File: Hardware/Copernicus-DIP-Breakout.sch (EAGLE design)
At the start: 12 parts, among them U1 COPERNICUS

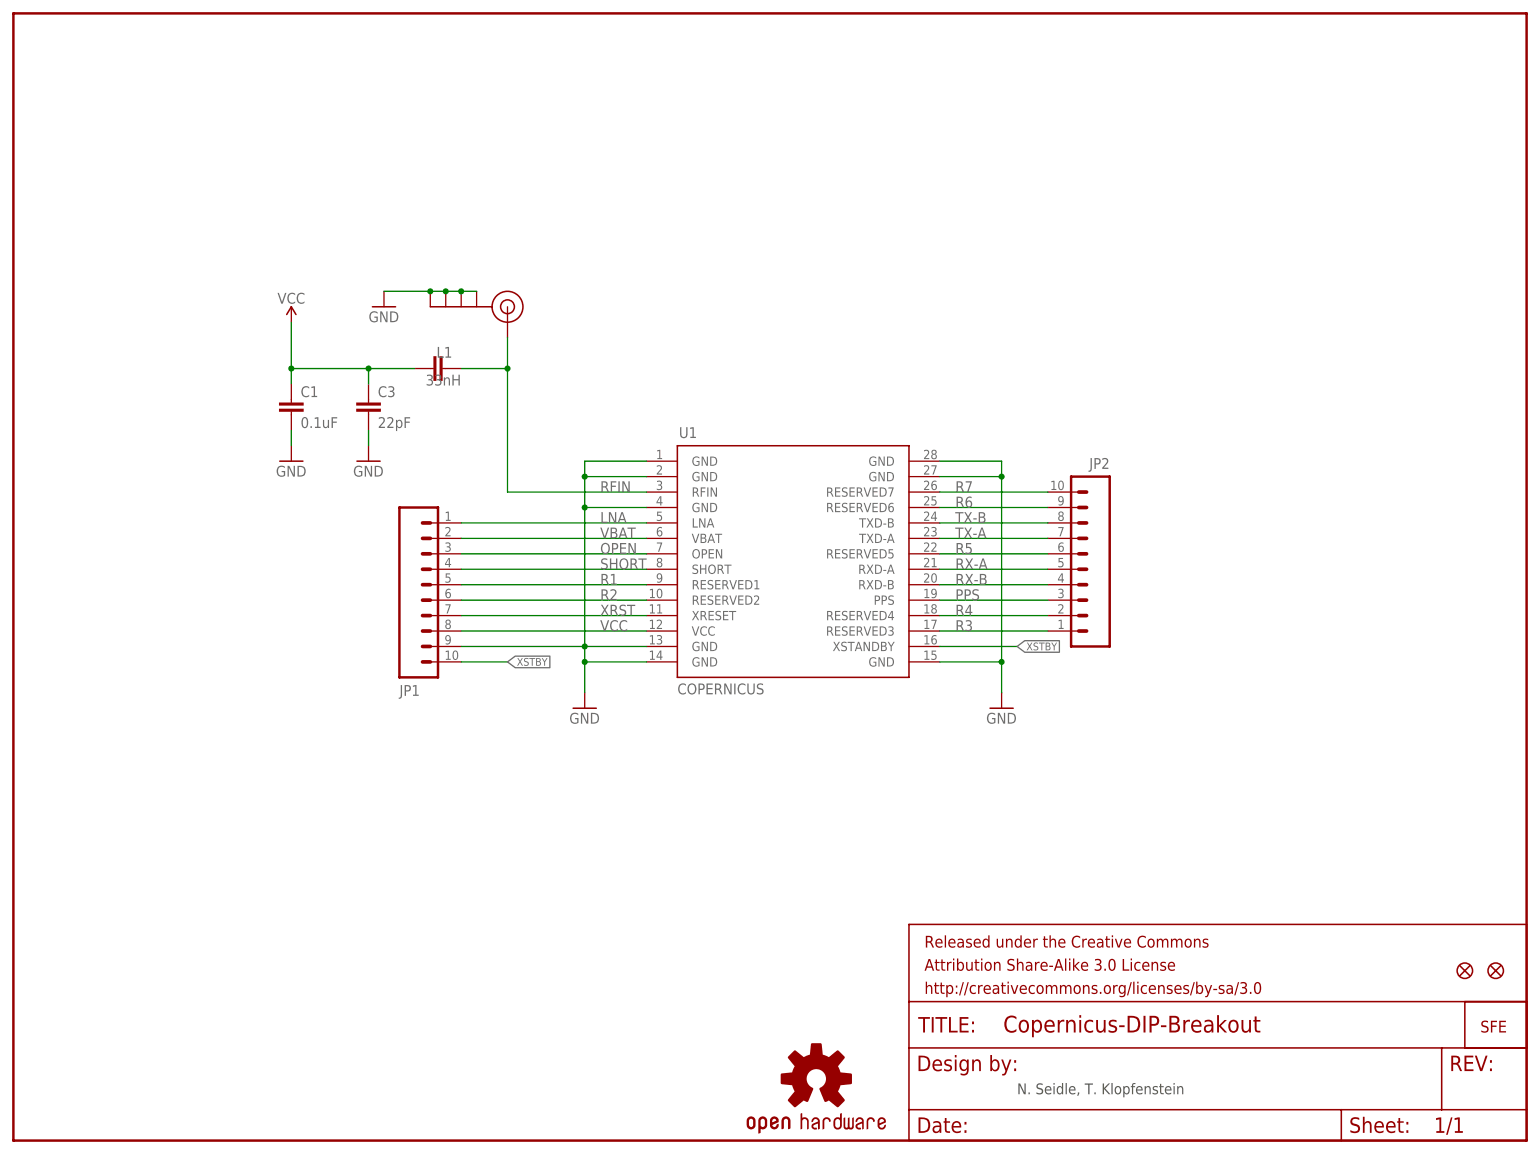
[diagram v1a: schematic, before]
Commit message: Updated board to proper pin names, added in connection between XSTBY and Vcc, changed caps and inductor to 0603 package, and decreased PCB size.
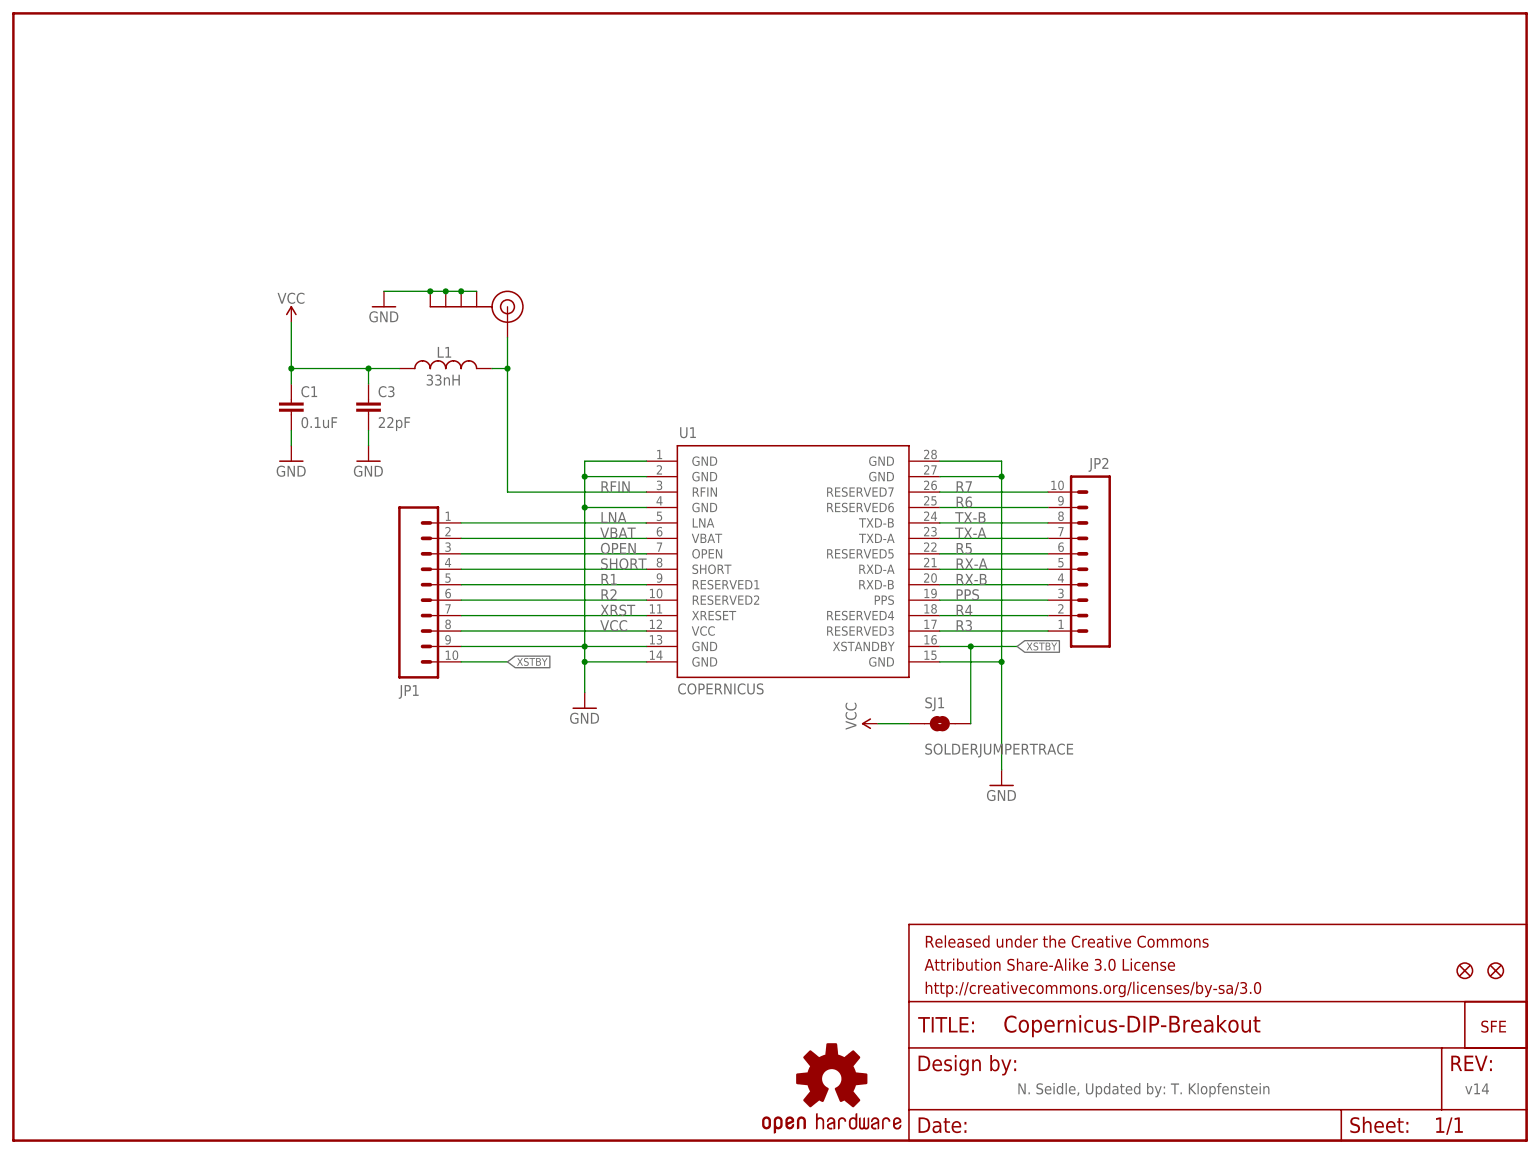
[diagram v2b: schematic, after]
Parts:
- removed LOGO1: OSHW-LOGOS, SparkFun-Aesthetics:OSHW-LOGOS
- added JP4: LOGO-SFESK, SparkFun-Aesthetics:LOGO-SFESK
- added SJ1: SOLDERJUMPERTRACE, SparkFun-Passives:SOLDERJUMPERTRACE
- C1, C3: device SparkFun:CAP0402-CAP -> SparkFun-Passives:CAP0603-CAP
- L1: device SparkFun:CAP0402-CAP -> SparkFun-Passives:INDUCTOR0603
- U$1: value LOGO-SFENEW -> OSHW-LOGOS; device SparkFun:LOGO-SFENEW -> SparkFun-Aesthetics:OSHW-LOGOS
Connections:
- net VCC: now also SJ1.1
- net XSTBY: now also SJ1.2
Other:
- note added: "N. Seidle, Updated by: T. Klopfenstein"
- note added: "v14"
- note removed: "N. Seidle, T. Klopfenstein"
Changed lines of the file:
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@@
 <parts>
 <part name="JP3" library="SparkFun-Nate" deviceset="SMA_EDGE" device=""/>
-<part name="C3" library="SparkFun" deviceset="CAP" device="0402-CAP" value="22pF"/>
-<part name="C1" library="SparkFun" deviceset="CAP" device="0402-CAP" value="0.1uF"/>
+<part name="C3" library="SparkFun-Passives" deviceset="CAP" device="0603-CAP" value="22pF"/>
+<part name="C1" library="SparkFun-Passives" deviceset="CAP" device="0603-CAP" value="0.1uF"/>
 <part name="3.3V1" library="SparkFun" deviceset="VCC" device=""/>
 <part name="GND9" library="SparkFun" deviceset="GND" device=""/>
@@
 <part name="JP2" library="SparkFun" deviceset="M10" device="&quot;" value=""/>
 <part name="U1" library="SparkFun-RF" deviceset="COPERNICUS" device="SMD" value="COPERNICUS"/>
-<part name="U$1" library="SparkFun" deviceset="LOGO-SFE" device="NEW"/>
 <part name="GND2" library="SparkFun" deviceset="GND" device=""/>
-<part name="L1" library="SparkFun" deviceset="CAP" device="0402-CAP" value="33nH"/>
+<part name="L1" library="SparkFun-Passives" deviceset="INDUCTOR" device="0603" value="33nH"/>
 <part name="U$2" library="SparkFun" deviceset="FIDUCIAL" device="1X2"/>
 <part name="U$3" library="SparkFun" deviceset="FIDUCIAL" device="1X2"/>
 <part name="GND1" library="SparkFun" deviceset="GND" device=""/>
 <part name="FRAME1" library="SparkFun-Aesthetics" deviceset="FRAME-LETTER" device=""/>
-<part name="LOGO1" library="SparkFun-Aesthetics" deviceset="OSHW-LOGO" device="S"/>
+<part name="SJ1" library="SparkFun-Passives" deviceset="SOLDERJUMPER" device="TRACE"/>
+<part name="P+1" library="SparkFun-Aesthetics" deviceset="VCC" device=""/>
+<part name="U$1" library="SparkFun-Aesthetics" deviceset="OSHW-LOGO" device="S"/>
+<part name="JP4" library="SparkFun-Aesthetics" deviceset="LOGO-SFE" device="SK"/>
 </parts>
 <sheets>
 <sheet>
 <plain>
-<text x="165.1" y="7.62" size="1.778" layer="97">N. Seidle, T. Klopfenstein</text>
+<text x="165.1" y="7.62" size="1.778" layer="96">N. Seidle, Updated by: T. Klopfenstein</text>
+<text x="238.76" y="7.62" size="1.778" layer="96">v14</text>
 </plain>
 <instances>
@@
 <attribute name="VALUE" x="109.22" y="73.406" size="1.778" layer="96"/>
 </instance>
-<instance part="U$1" gate="G$1" x="241.3" y="17.78"/>
 <instance part="GND2" gate="1" x="93.98" y="71.12"/>
 <instance part="L1" gate="G$1" x="71.12" y="127" smashed="yes" rot="R90">
@@
 <instance part="U$2" gate="G$1" x="243.84" y="27.94"/>
 <instance part="U$3" gate="G$1" x="238.76" y="27.94"/>
-<instance part="GND1" gate="1" x="162.56" y="71.12"/>
+<instance part="GND1" gate="1" x="162.56" y="58.42"/>
 <instance part="FRAME1" gate="G$1" x="0" y="0"/>
 <instance part="FRAME1" gate="G$2" x="147.32" y="0"/>
-<instance part="LOGO1" gate="G$1" x="132.08" y="10.16"/>
+<instance part="SJ1" gate="1" x="152.4" y="68.58"/>
+<instance part="P+1" gate="1" x="142.24" y="68.58" rot="R90"/>
+<instance part="U$1" gate="G$1" x="134.62" y="10.16"/>
+<instance part="JP4" gate="G$1" x="241.3" y="17.78"/>
 </instances>
 <busses>
@@
 <segment>
 <pinref part="GND1" gate="1" pin="GND"/>
-<wire x1="162.56" y1="78.74" x2="162.56" y2="73.66" width="0.1524" layer="91"/>
+<wire x1="162.56" y1="78.74" x2="162.56" y2="60.96" width="0.1524" layer="91"/>
 <wire x1="162.56" y1="78.74" x2="152.4" y2="78.74" width="0.1524" layer="91"/>
 <pinref part="U1" gate="G$2" pin="GND@6"/>
@@
 </segment>
 <segment>
-<wire x1="66.04" y1="127" x2="58.42" y2="127" width="0.1524" layer="91"/>
+<wire x1="63.5" y1="127" x2="58.42" y2="127" width="0.1524" layer="91"/>
 <wire x1="58.42" y1="127" x2="45.72" y2="127" width="0.1524" layer="91"/>
 <wire x1="45.72" y1="127" x2="45.72" y2="134.62" width="0.1524" layer="91"/>
@@
 <pinref part="L1" gate="G$1" pin="1"/>
 </segment>
+<segment>
+<pinref part="SJ1" gate="1" pin="1"/>
+<pinref part="P+1" gate="1" pin="VCC"/>
+<wire x1="142.24" y1="68.58" x2="147.32" y2="68.58" width="0.1524" layer="91"/>
+</segment>
 </net>
 <net name="RFIN" class="0">
 <segment>
 <wire x1="81.28" y1="127" x2="81.28" y2="132.08" width="0.1524" layer="91"/>
-<wire x1="73.66" y1="127" x2="81.28" y2="127" width="0.1524" layer="91"/>
+<wire x1="78.74" y1="127" x2="81.28" y2="127" width="0.1524" layer="91"/>
 <wire x1="104.14" y1="106.68" x2="81.28" y2="106.68" width="0.1524" layer="91"/>
 <wire x1="81.28" y1="106.68" x2="81.28" y2="127" width="0.1524" layer="91"/>
@@
 <net name="XSTBY" class="0">
 <segment>
-<wire x1="165.1" y1="81.28" x2="152.4" y2="81.28" width="0.1524" layer="91"/>
+<wire x1="165.1" y1="81.28" x2="157.48" y2="81.28" width="0.1524" layer="91"/>
 <pinref part="U1" gate="G$2" pin="XSTANDBY"/>
-<label x="165.1" y="81.28" size="1.27" layer="91" xref="yes"/>
+<label x="165.1" y="81.28" size="1.27" layer="95" xref="yes"/>
+<wire x1="157.48" y1="81.28" x2="152.4" y2="81.28" width="0.1524" layer="91"/>
+<wire x1="157.48" y1="81.28" x2="157.48" y2="68.58" width="0.1524" layer="91"/>
+<junction x="157.48" y="81.28"/>
+<pinref part="SJ1" gate="1" pin="2"/>
 </segment>
 <segment>
 <wire x1="73.66" y1="78.74" x2="81.28" y2="78.74" width="0.1524" layer="91"/>
 <pinref part="JP1" gate="G$1" pin="10"/>
-<label x="81.28" y="78.74" size="1.27" layer="91" xref="yes"/>
-</segment>
-</net>
+<label x="81.28" y="78.74" size="1.27" layer="95" xref="yes"/>
+</segment>
+</net>
